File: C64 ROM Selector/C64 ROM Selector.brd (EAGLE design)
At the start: 62.2 x 56.8 mm, 6 parts, among them IC1 2364, IC2 27256

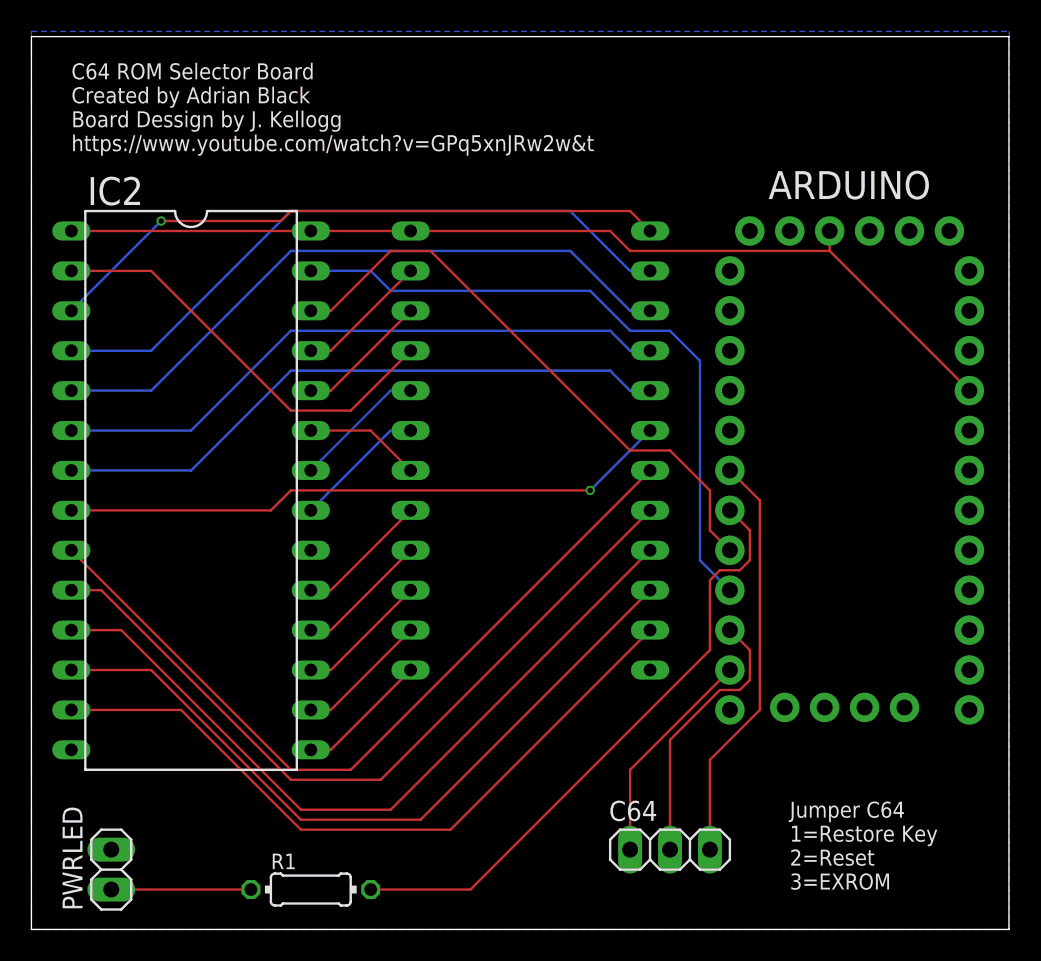
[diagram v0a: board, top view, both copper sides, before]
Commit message: Minor edits to labels
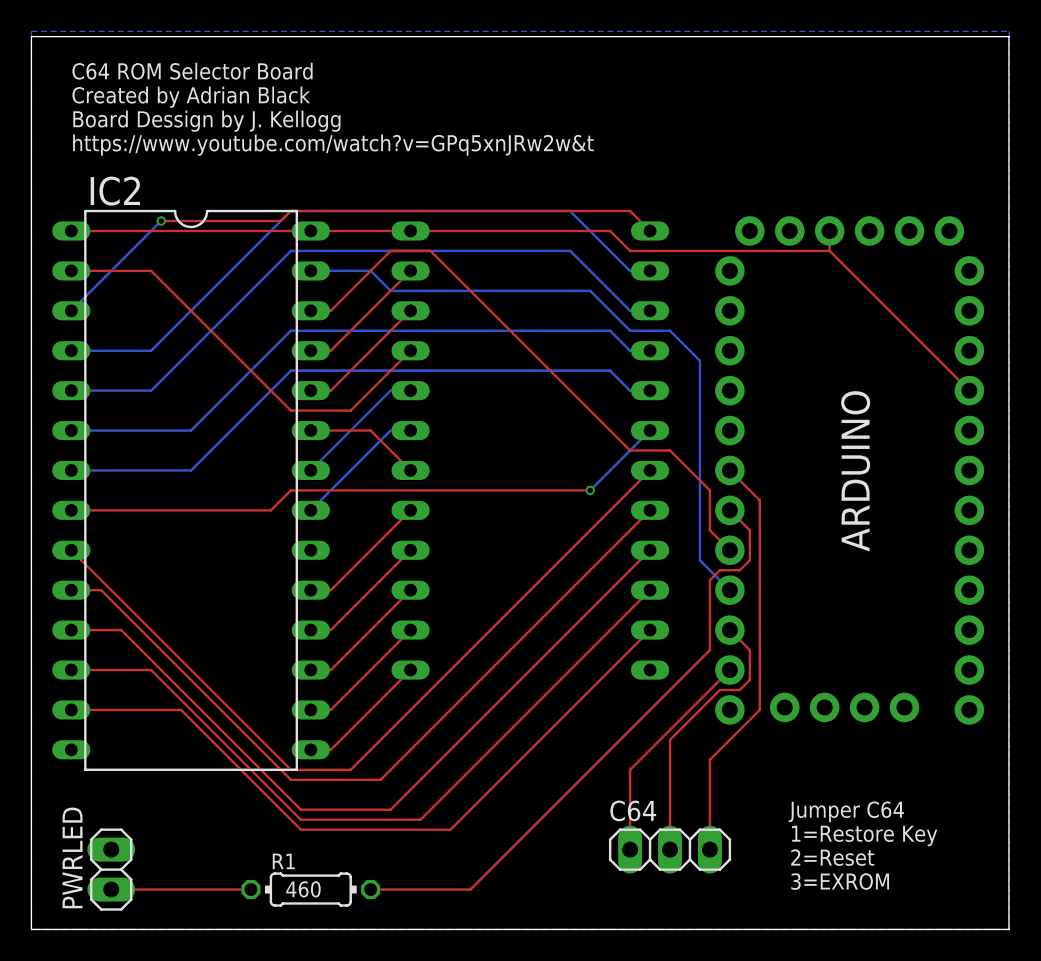
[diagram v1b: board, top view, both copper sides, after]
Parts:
- IC1: value 2364 -> C64 ROM SOCKET
- IC2: value 27256 -> 27256 EEPROM
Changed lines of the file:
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@@
 </element>
 <element name="ARDUINO" library="myparts" package="ARDUINO_PRO_MINI" value="ADR_PROMINI" x="54.61" y="27.94" smashed="yes">
-<attribute name="NAME" x="54.61" y="45.212" size="1.778" layer="25" ratio="20" align="bottom-center"/>
+<attribute name="NAME" x="54.102" y="27.94" size="1.778" layer="21" ratio="20" rot="R270" align="bottom-center"/>
 <attribute name="VALUE" x="54.61" y="11.049" size="1.778" layer="27" ratio="20" align="top-center"/>
 </element>
@@
 <attribute name="POPULARITY" value="48" x="20.32" y="1.27" size="1.778" layer="27" display="off"/>
 <attribute name="SPICEPREFIX" value="R" x="20.32" y="1.27" size="1.778" layer="27" display="off"/>
-<attribute name="VALUE" x="18.6944" y="0.7874" size="0.9906" layer="27" ratio="10"/>
+<attribute name="VALUE" x="18.6944" y="0.7874" size="0.9906" layer="21" ratio="10"/>
 </element>
-<element name="IC1" library="myparts" package="DIL24" package3d_urn="urn:adsk.eagle:package:19955/2" value="2364" x="34.29" y="29.21" smashed="yes" rot="MR270">
+<element name="IC1" library="myparts" package="DIL24" package3d_urn="urn:adsk.eagle:package:19955/2" value="C64 ROM SOCKET" x="34.29" y="29.21" smashed="yes" rot="MR270">
 <attribute name="NAME" x="41.021" y="44.704" size="1.778" layer="26" ratio="10" rot="MR0"/>
 <attribute name="POPULARITY" value="0" x="34.29" y="29.21" size="1.778" layer="28" rot="MR270" display="off"/>
-<attribute name="VALUE" x="35.179" y="40.513" size="1.778" layer="28" ratio="10" rot="MR270"/>
+<attribute name="VALUE" x="35.179" y="40.513" size="1.778" layer="22" ratio="10" rot="MR270"/>
 </element>
-<element name="IC2" library="myparts" package="DIL28" package3d_urn="urn:adsk.eagle:package:31069/1" value="27256" x="12.7" y="26.67" smashed="yes" rot="R270">
+<element name="IC2" library="myparts" package="DIL28" package3d_urn="urn:adsk.eagle:package:31069/1" value="27256 EEPROM" x="12.7" y="26.67" smashed="yes" rot="R270">
 <attribute name="NAME" x="6.096" y="44.831" size="1.778" layer="25"/>
 <attribute name="POPULARITY" value="1" x="12.7" y="26.67" size="1.778" layer="27" rot="R270" display="off"/>
